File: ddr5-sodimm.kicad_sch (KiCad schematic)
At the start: 3 parts, among them J4001 BUS_DDR5_SODIMM_AMPHENOL_1016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

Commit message: Add loclib
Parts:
- C401: footprint antmicro-footprints:C_0402_1005Metric -> sodimm-ddr5-tester-footprints:C_0402_1005Metric; symbol Capacitors0402:C_100n_0402 -> sodimm-ddr5-tester:C_100n_0402
- C402: footprint data-center-rdimm-ddr4-tester-footprints:C_0402_1005Metric -> sodimm-ddr5-tester-footprints:C_0402_1005Metric; symbol data-center-rdimm-ddr4-tester:C_4u7_0402 -> sodimm-ddr5-tester:C_4u7_0402
- J4001: footprint antmicro-footprints:DDR5_AMPHENOL_10161033-002RHLF -> sodimm-ddr5-tester-footprints:DDR5_AMPHENOL_10161033-002RHLF; symbol antmicroMemoryConnectorsPCCardSockets:BUS_DDR5_SODIMM_AMPHENOL_10161033-002RHLF -> sodimm-ddr5-tester:BUS_DDR5_SODIMM_AMPHENOL_10161033-002RHLF

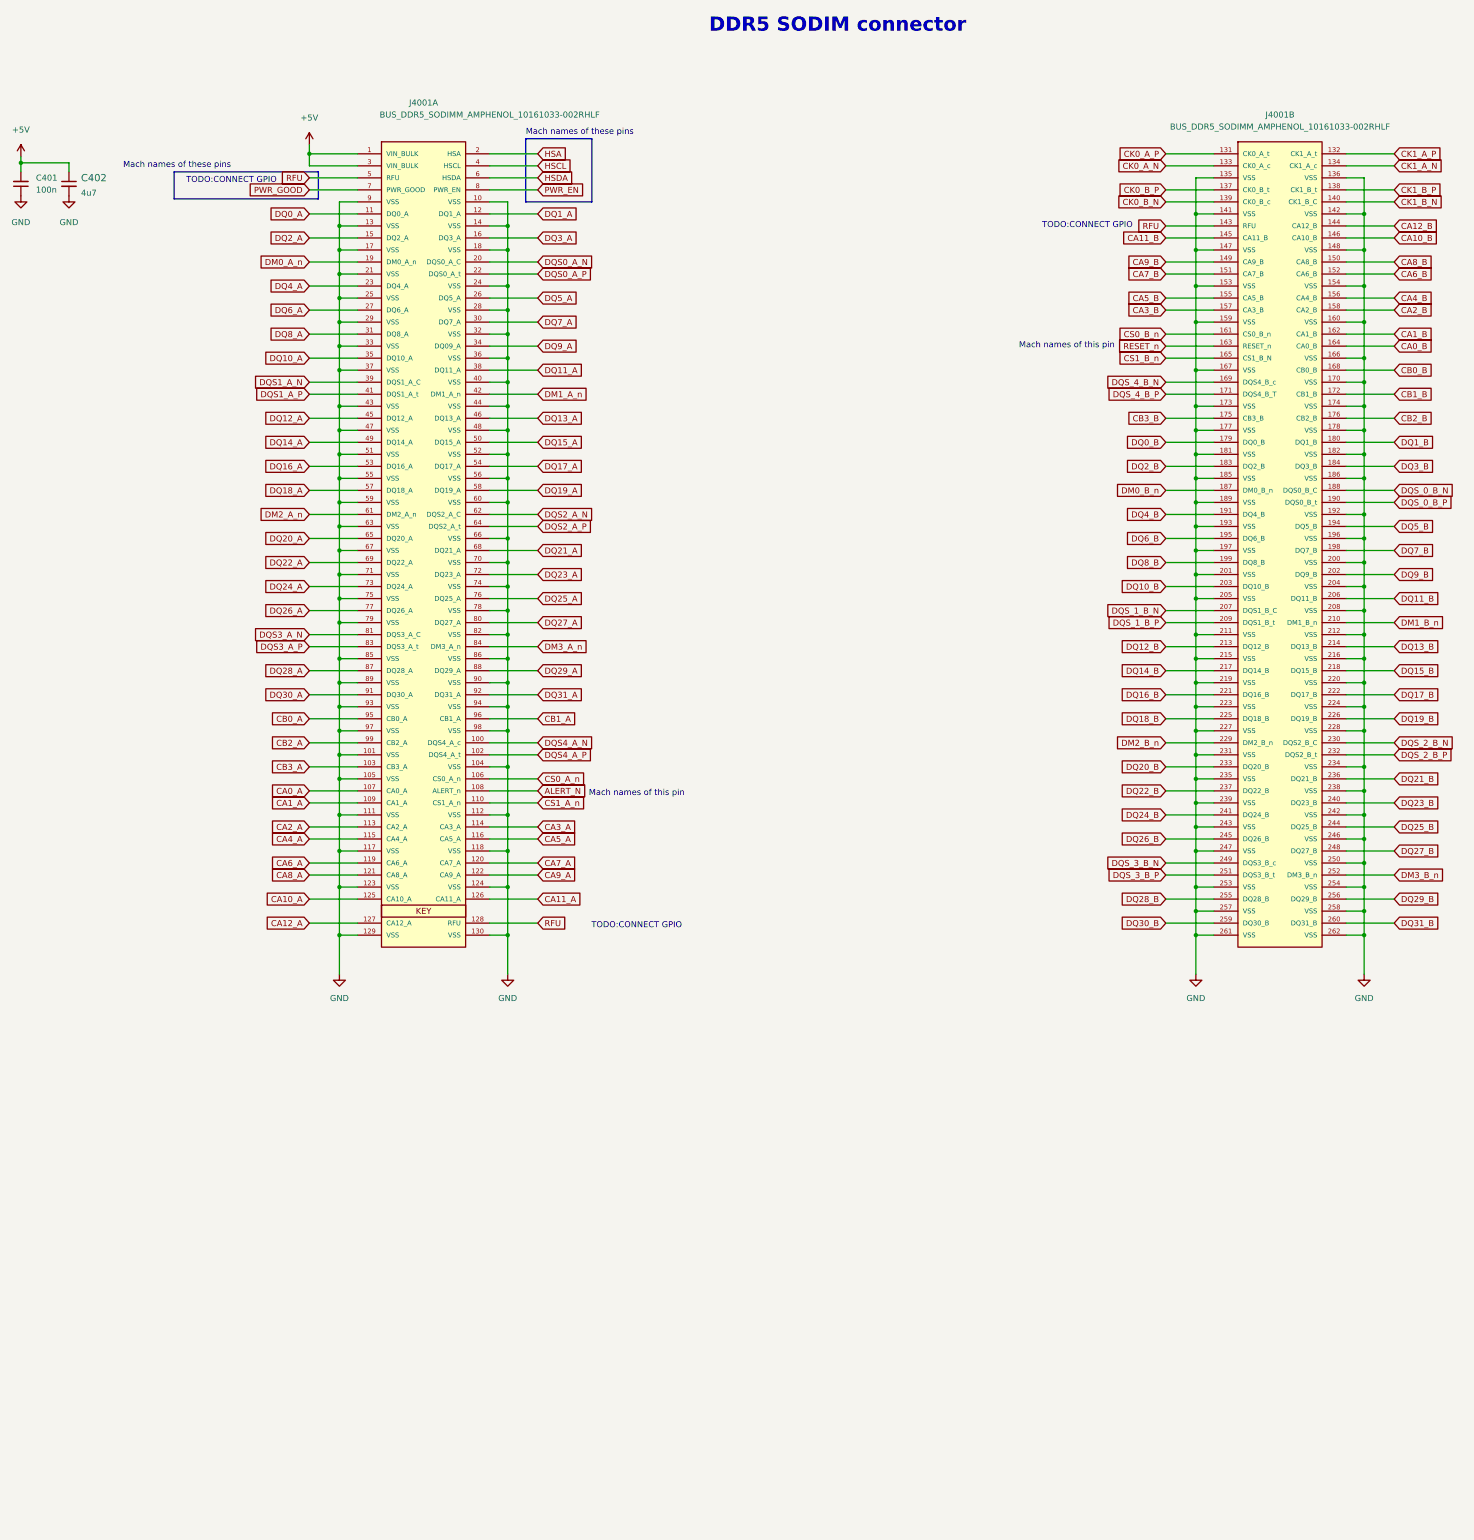
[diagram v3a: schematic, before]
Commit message: Finalize routing
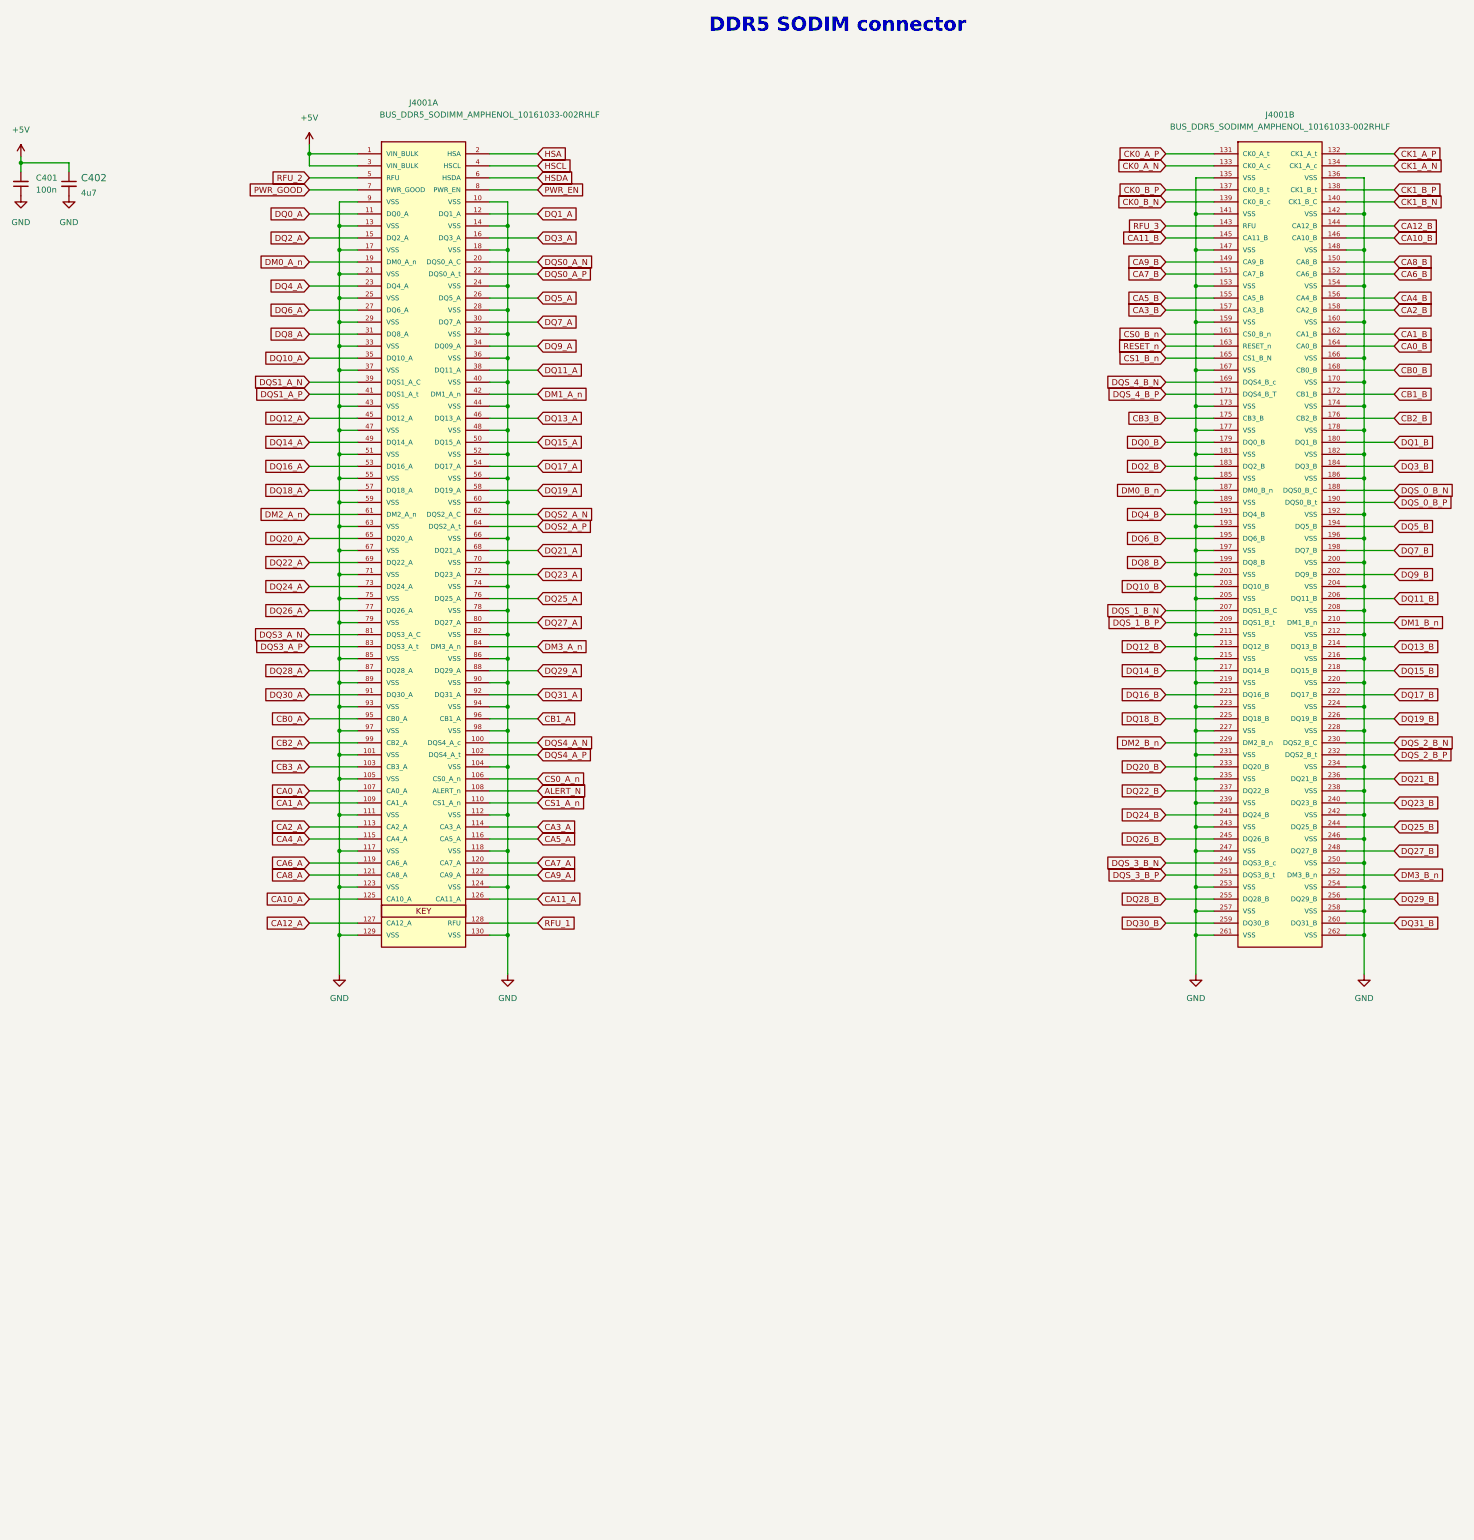
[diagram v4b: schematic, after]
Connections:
- removed net RFU: J4001.128 (RFU), J4001.143 (RFU), J4001.5 (RFU)
- new net RFU_1: J4001.128 (RFU)
- new net RFU_2: J4001.5 (RFU)
- new net RFU_3: J4001.143 (RFU)
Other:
- note removed: "Mach names of these pins"
- note removed: "Mach names of this pin"
- note removed: "TODO:CONNECT GPIO"

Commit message: Bump revision to 1.0.0
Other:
- title: LPDDR5 Test Board -> SO-DIMM DDR5 Tester
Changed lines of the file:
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@@
   (paper "A3")
   (title_block
-    (title "LPDDR5 Test Board")
-    (date "2023-12-18")
-    (rev "0.0.99")
+    (title "SO-DIMM DDR5 Tester")
+    (date "2023-12")
+    (rev "1.0.0")
     (company "Antmicro Ltd.")
     (comment 1 "www.antmicro.com")

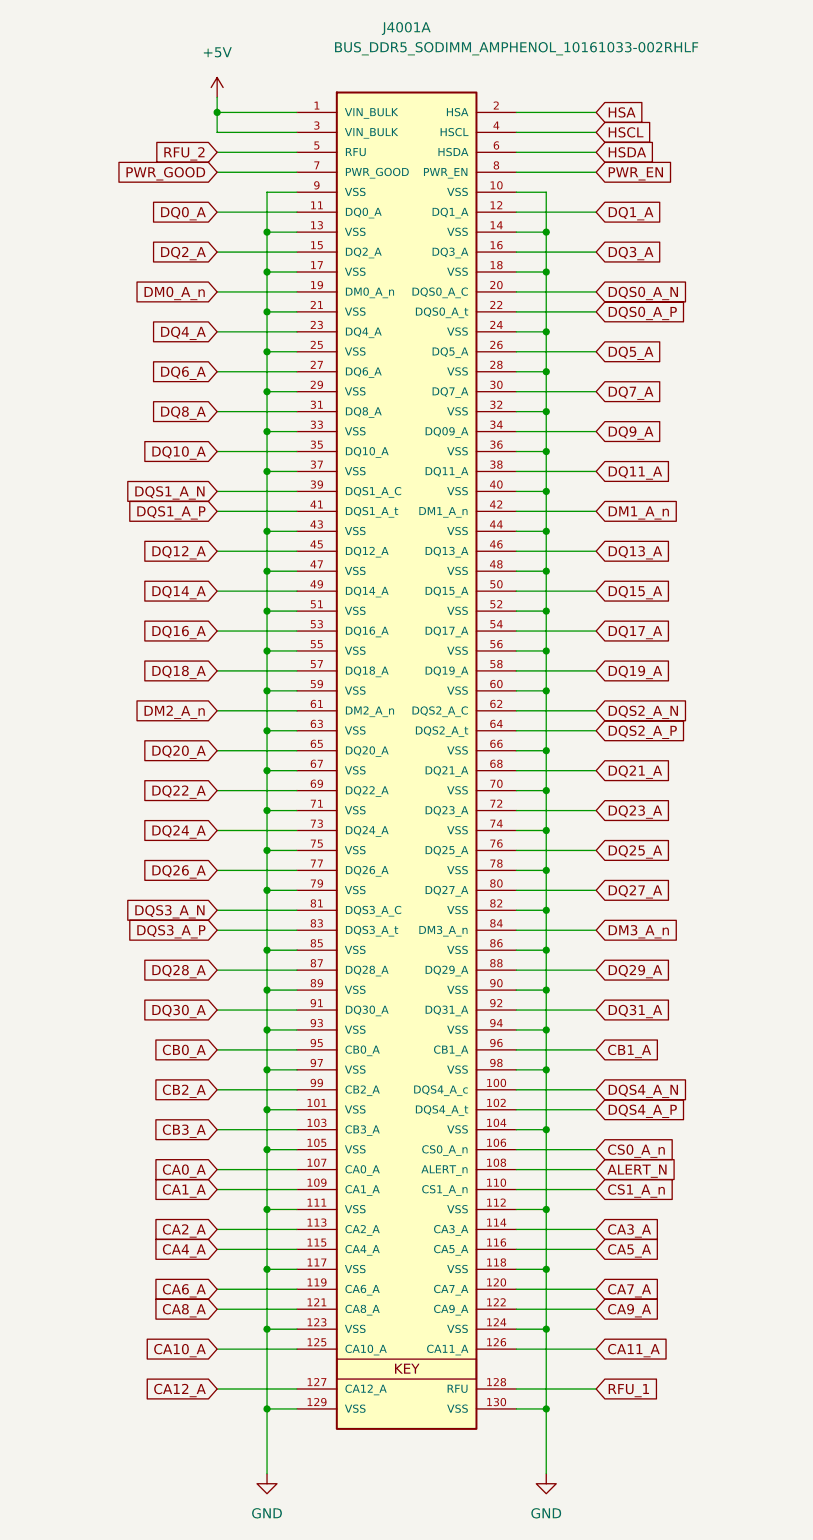
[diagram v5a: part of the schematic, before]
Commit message: Connect RFU, start improving interfaces and supply sheet, unify ESD protection
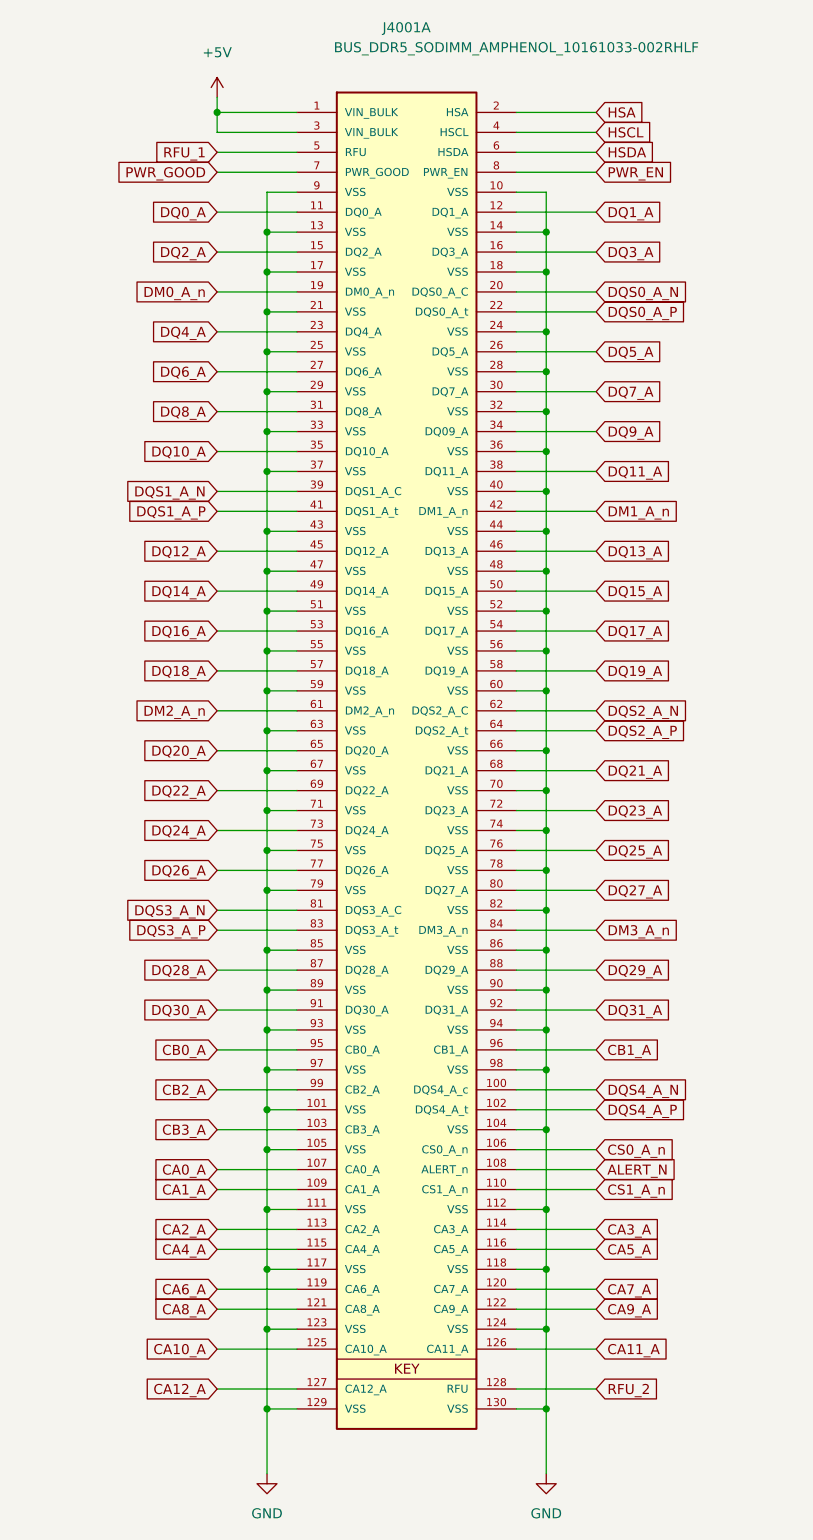
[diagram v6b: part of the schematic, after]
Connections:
- net RFU_1: now also J4001.5 (RFU); no longer J4001.128 (RFU)
- net RFU_2: now also J4001.128 (RFU); no longer J4001.5 (RFU)
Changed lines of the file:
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@@
     )
   )
-  (global_label "RFU_2" (shape input) (at 89.535 56.515 180) (fields_autoplaced)
+  (global_label "RFU_1" (shape input) (at 89.535 56.515 180) (fields_autoplaced)
     (effects (font (size 1.27 1.27)) (justify right))
     (property "Intersheet References" "${INTERSHEET_REFS}" (id 0) (at 81.3446 56.4356 0)
@@
     )
   )
-  (global_label "RFU_1" (shape input) (at 137.795 213.995 0) (fields_autoplaced)
+  (global_label "RFU_2" (shape input) (at 137.795 213.995 0) (fields_autoplaced)
     (effects (font (size 1.27 1.27)) (justify left))
     (property "Intersheet References" "${INTERSHEET_REFS}" (id 0) (at 145.9854 213.9156 0)
